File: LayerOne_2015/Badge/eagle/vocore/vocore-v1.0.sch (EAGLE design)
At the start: 2 parts

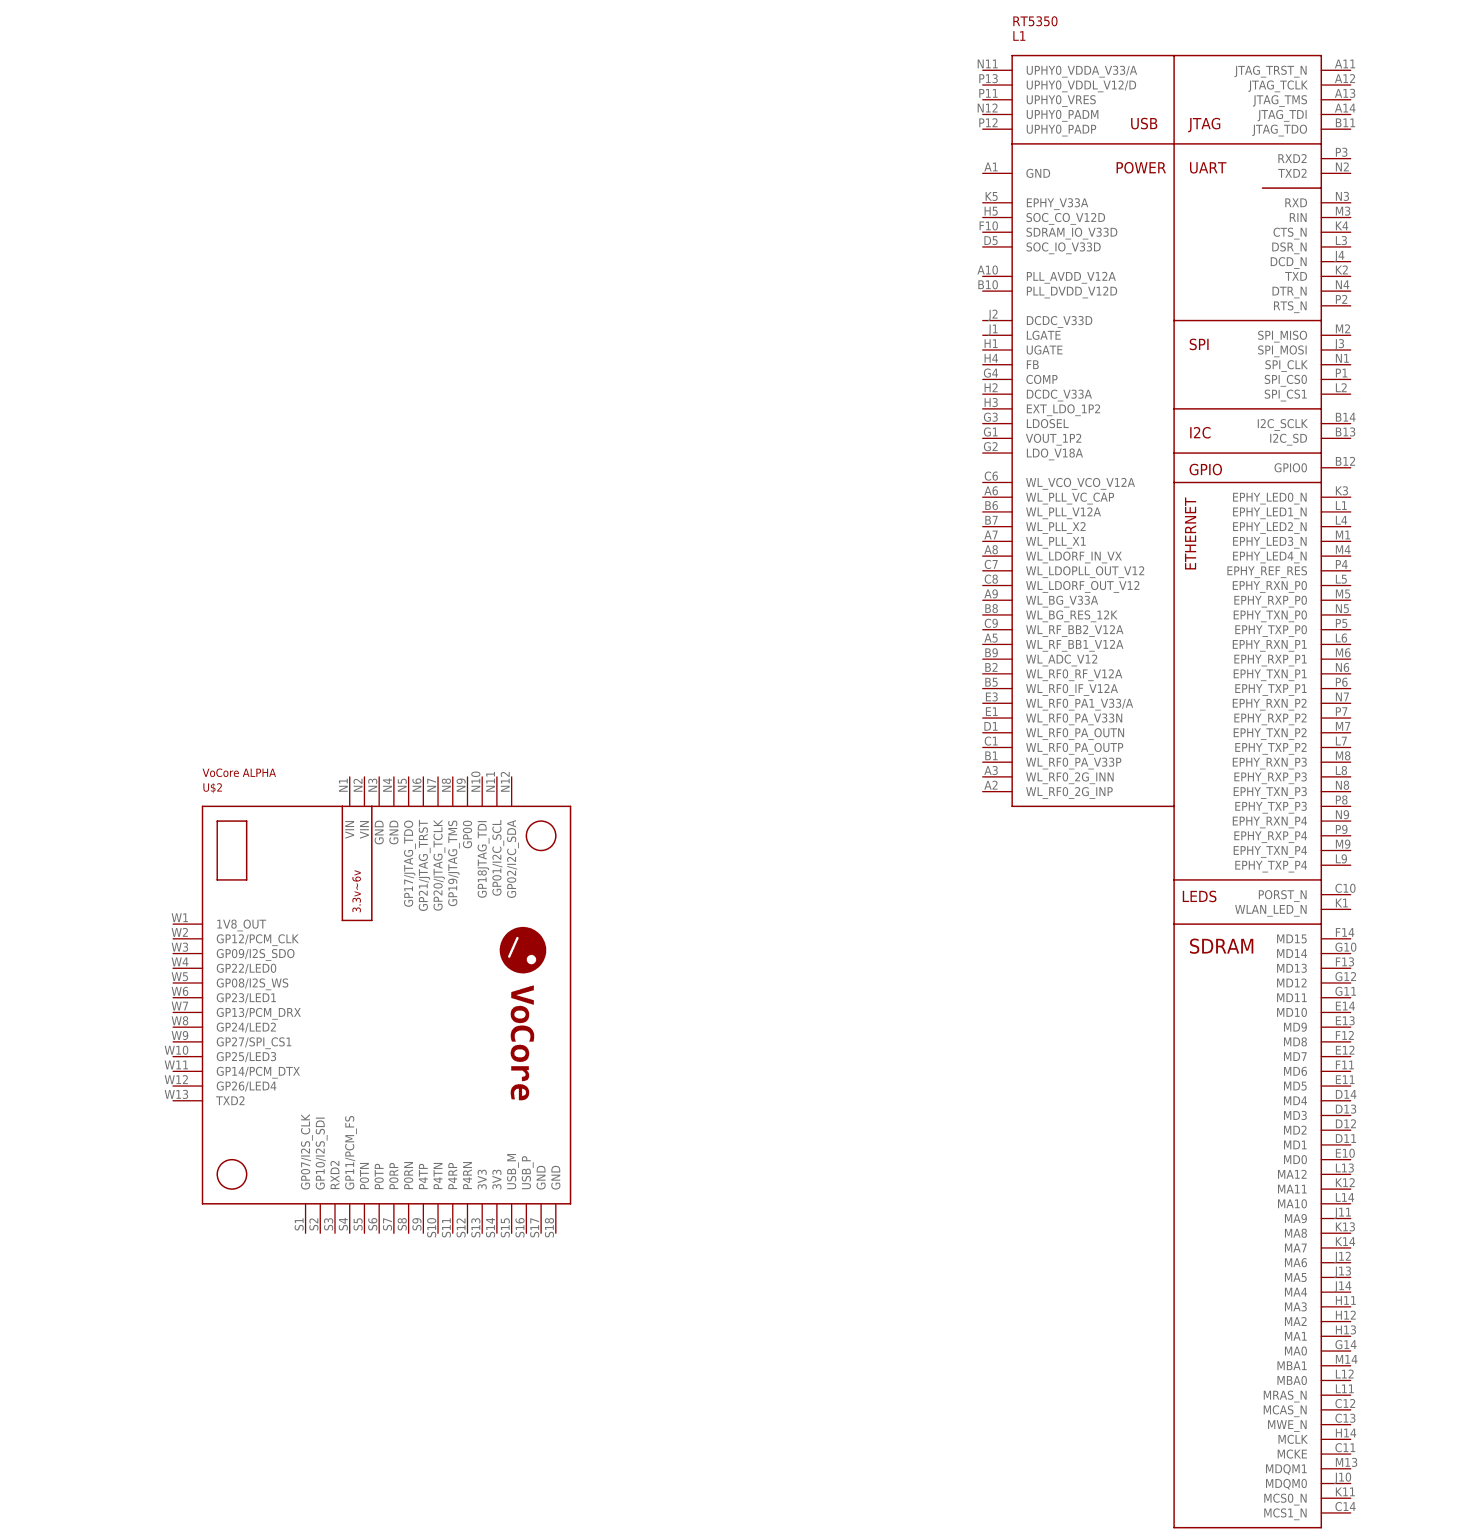
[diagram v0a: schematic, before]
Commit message: 
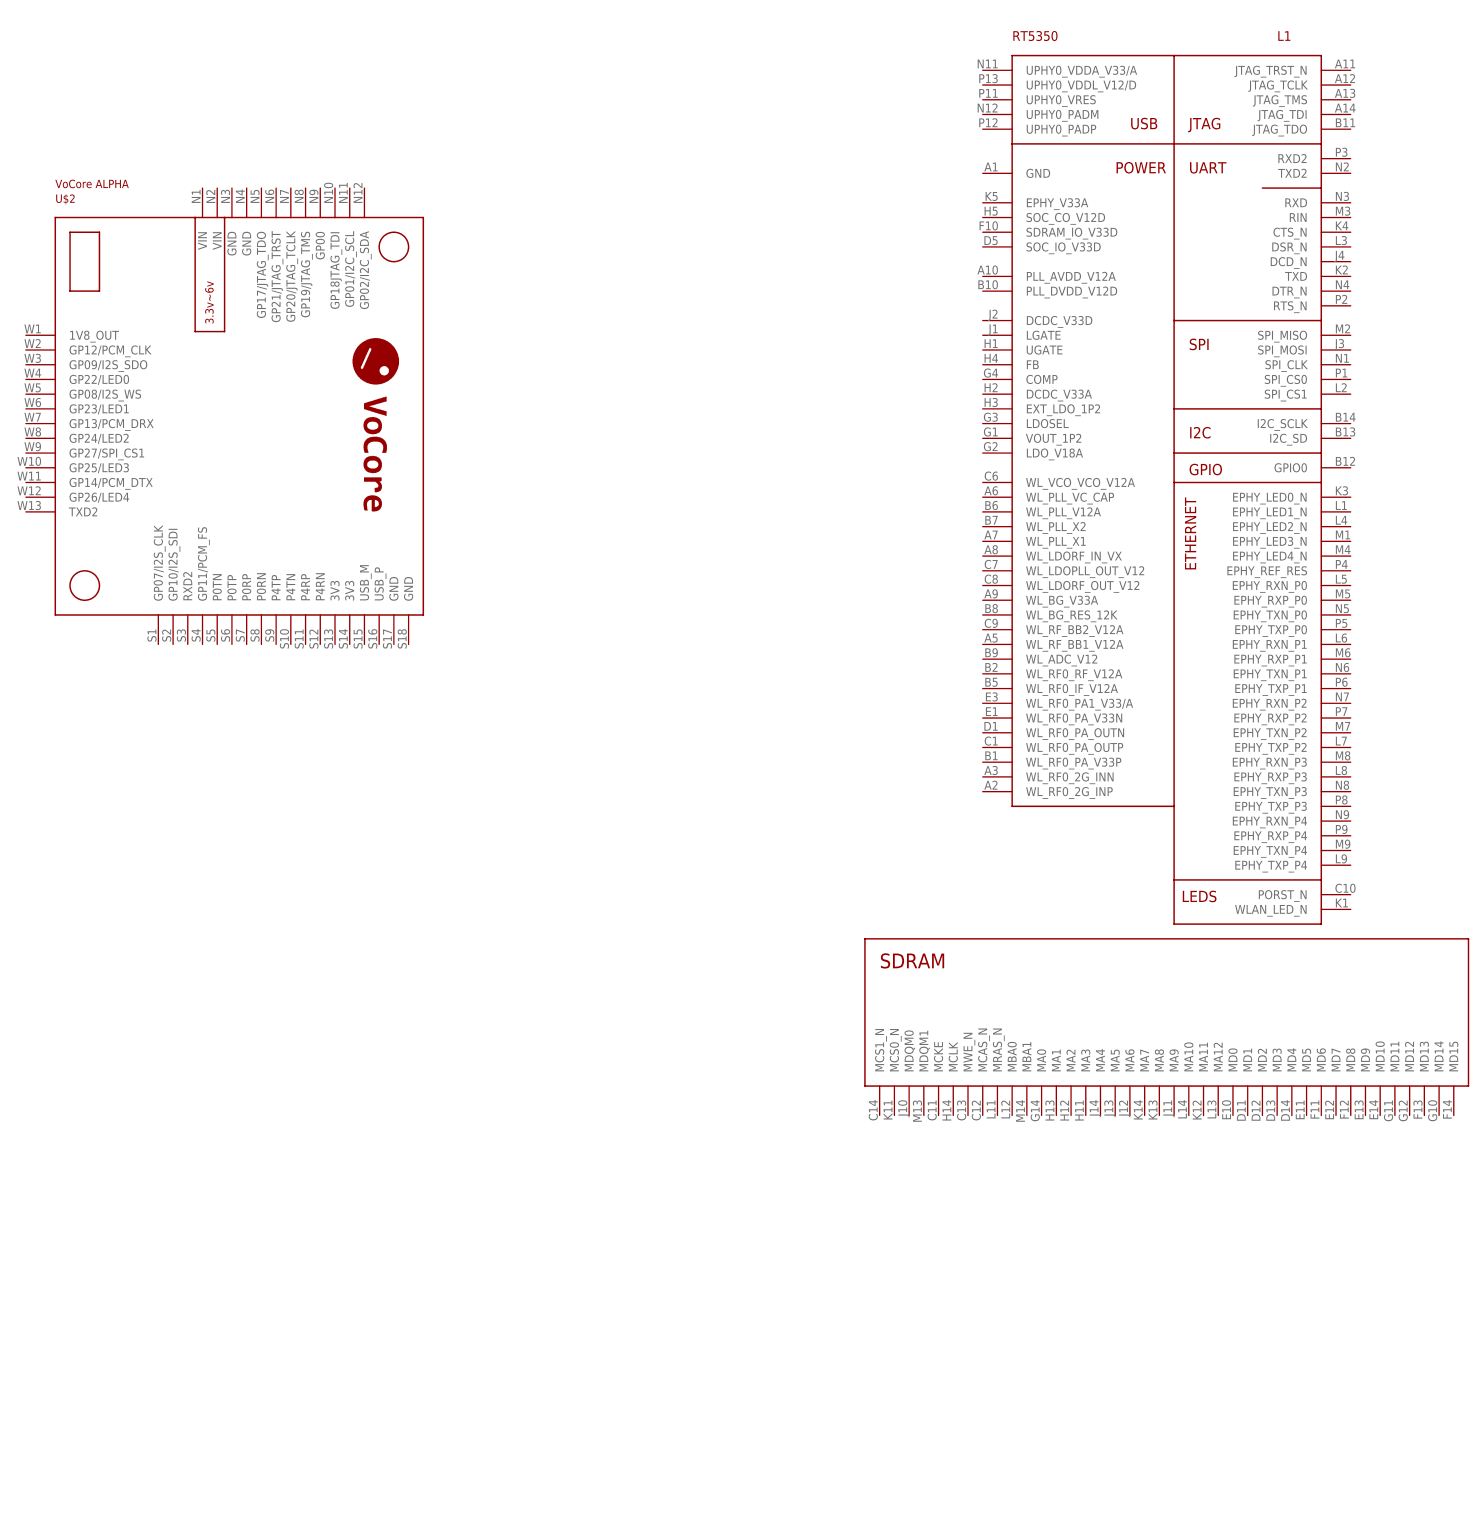
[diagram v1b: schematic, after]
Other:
- moved on the sheet: U$2
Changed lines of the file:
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@@
 </plain>
 <instances>
-<instance part="U$2" gate="MOD$1" x="-20.32" y="43.18"/>
+<instance part="U$2" gate="MOD$1" x="-45.72" y="144.78"/>
 <instance part="L1" gate="G$1" x="111.76" y="76.2"/>
 </instances>
